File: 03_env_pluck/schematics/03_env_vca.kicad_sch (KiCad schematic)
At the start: 66 parts, among them J1 Eurorack 10 pin power connect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, J1 Gate In 1, J2 Signal in In 1, J3 Gate In 1, J4 Env Out 1, J4 signal out, J5 Env Out 1, Q1 BC547, Q2 BC547, SW1 Pluck / AD, SW2 Pluck / AD, U1 TL072, U2 LM324

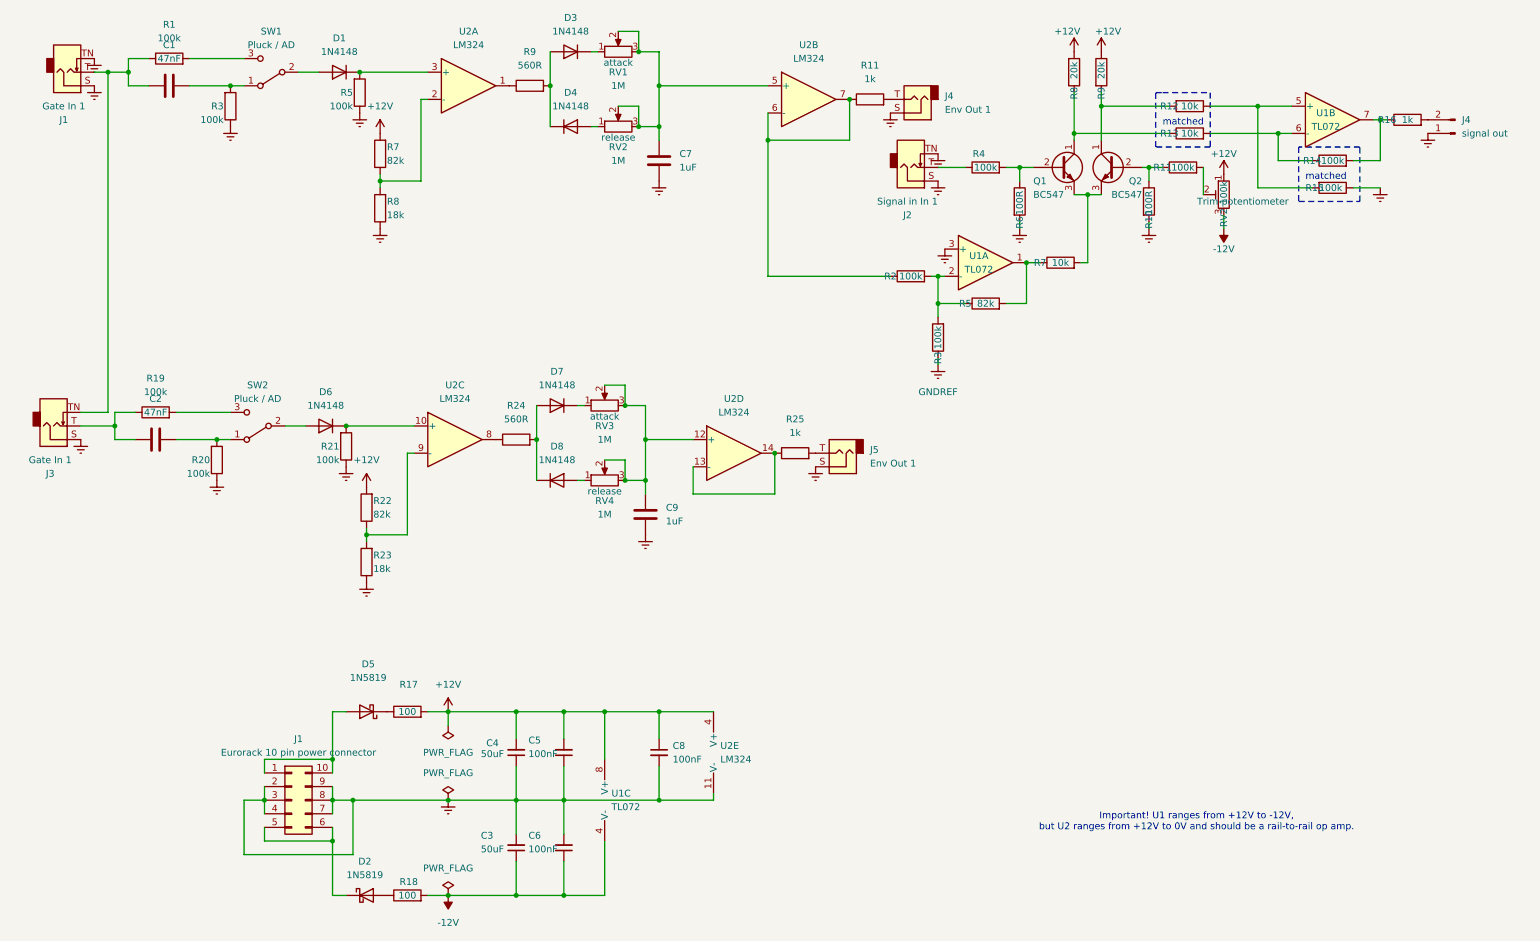
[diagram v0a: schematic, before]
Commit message: added PCB for 03
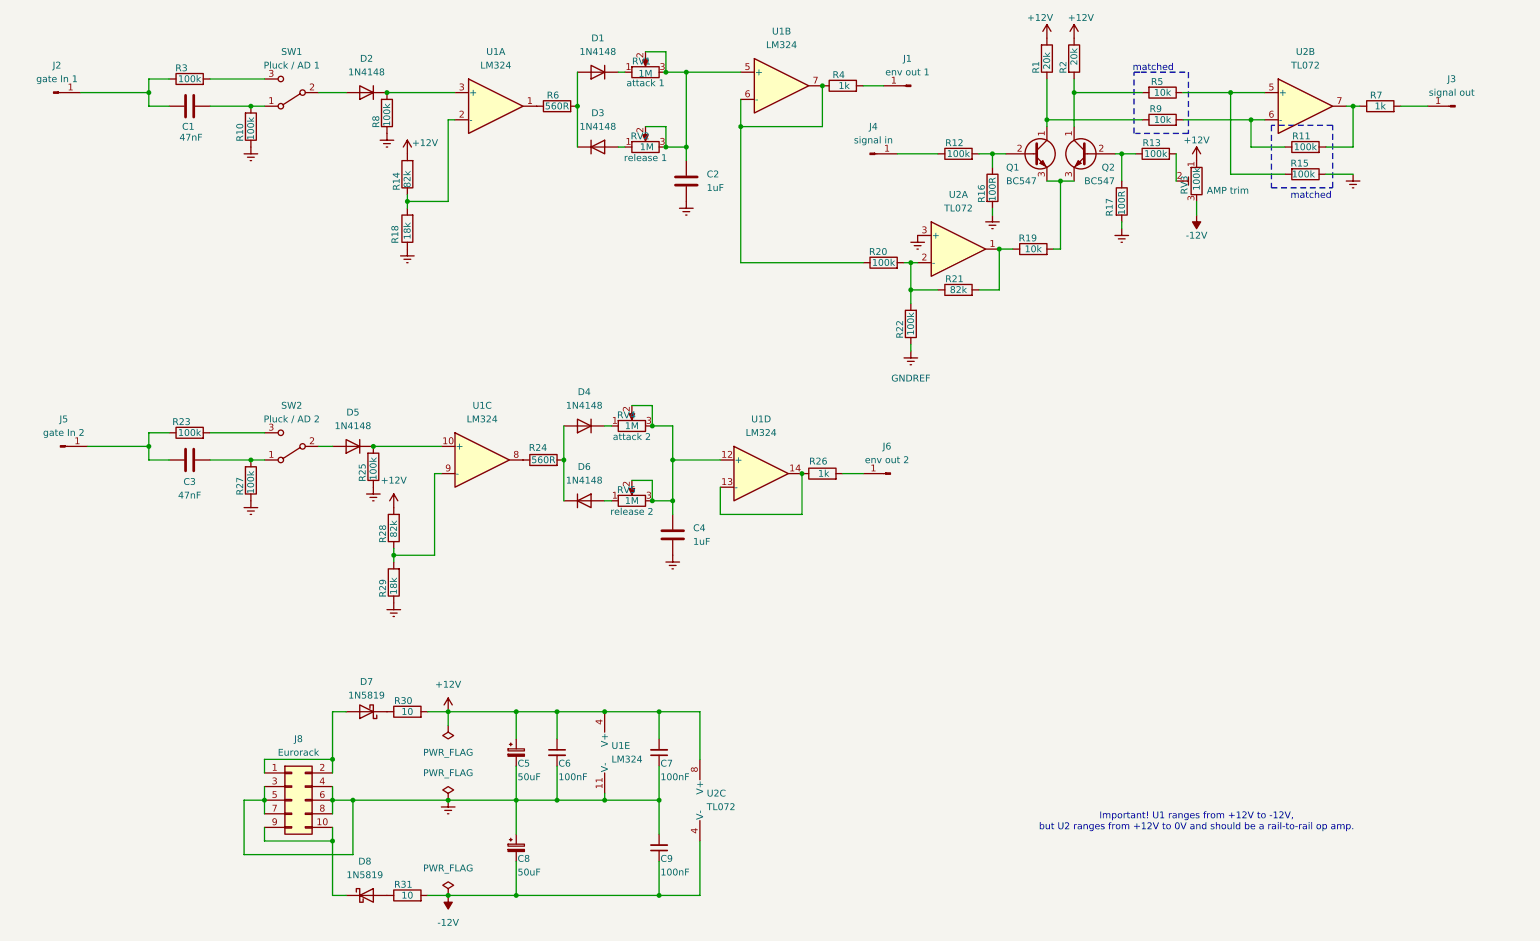
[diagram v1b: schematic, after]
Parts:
- removed C3, C4: 50uF, Capacitor_THT:C_Disc_D6.0mm_W2.5mm_P5.00mm, symbol Device:C_Small
- removed J1, J3: Gate In 1, Connector_Audio:Jack_6.35mm_Neutrik_NJ5FD-V_Vertical, symbol Connector_Audio:AudioJack2_SwitchT
- removed J1: Eurorack 10 pin power connector, Connector_PinHeader_2.54mm:PinHeader_2x05_P2.54mm_Vertical, symbol Connector_Generic:Conn_02x05_Counter_Clockwise
- removed J2: Signal in In 1, Connector_Audio:Jack_6.35mm_Neutrik_NJ5FD-V_Vertical, symbol Connector_Audio:AudioJack2_SwitchT
- removed J4, J5: Env Out 1, Connector_Audio:Jack_6.35mm_Neutrik_NJ5FD-V_Vertical, symbol Connector:AudioJack2
- removed J4: signal out, Connector_PinHeader_2.54mm:PinHeader_1x02_P2.54mm_Vertical, symbol Connector:Conn_01x02_Pin
- removed U1: TL072, Package_DIP:DIP-8_W7.62mm_Socket, symbol Amplifier_Operational:TL072
- added C5, C8: 50uF, Capacitor_THT:CP_Radial_D6.3mm_P2.50mm, symbol Device:C_Polarized_Small
- added J1: env out 1, Connector_PinHeader_2.54mm:PinHeader_1x01_P2.54mm_Vertical, symbol Connector:Conn_01x01_Pin
- added J2: gate In 1, Connector_PinHeader_2.54mm:PinHeader_1x01_P2.54mm_Vertical, symbol Connector:Conn_01x01_Pin
- added J3: signal out, Connector_PinHeader_2.54mm:PinHeader_1x01_P2.54mm_Vertical, symbol Connector:Conn_01x01_Pin
- added J4: signal in, Connector_PinHeader_2.54mm:PinHeader_1x01_P2.54mm_Vertical, symbol Connector:Conn_01x01_Pin
- added J5: gate In 2, Connector_PinHeader_2.54mm:PinHeader_1x01_P2.54mm_Vertical, symbol Connector:Conn_01x01_Pin
- added J6: env out 2, Connector_PinHeader_2.54mm:PinHeader_1x01_P2.54mm_Vertical, symbol Connector:Conn_01x01_Pin
- added J8: Eurorack, Connector_PinHeader_2.54mm:PinHeader_2x05_P2.54mm_Vertical, symbol Connector_Generic:Conn_02x05_Odd_Even
- added U2: TL072, Package_DIP:DIP-8_W7.62mm_Socket, symbol Amplifier_Operational:TL072
- R30: renamed from R17; value 100 -> 10
- R31: renamed from R18; value 100 -> 10
- RV1, RV2: footprint Potentiometer_THT:Potentiometer_Alpha_RD901F-40-00D_Single_Vertical -> Connector_PinHeader_2.54mm:PinHeader_1x03_P2.54mm_Vertical
- RV4: renamed from RV3; footprint Potentiometer_THT:Potentiometer_Alpha_RD901F-40-00D_Single_Vertical -> Connector_PinHeader_2.54mm:PinHeader_1x03_P2.54mm_Vertical
- RV5: renamed from RV4; footprint Potentiometer_THT:Potentiometer_Alpha_RD901F-40-00D_Single_Vertical -> Connector_PinHeader_2.54mm:PinHeader_1x03_P2.54mm_Vertical
- SW1: value Pluck / AD -> Pluck / AD 1
- SW2: value Pluck / AD -> Pluck / AD 2
- U1: renamed from U2; footprint (none) -> Package_DIP:DIP-14_W7.62mm_Socket
- renumbered C7 to C2, C2 to C3, C9 to C4, C8 to C6, C5 to C7, C6 to C9, D3 to D1, D1 to D2, D4 to D3, D7 to D4, D6 to D5, D8 to D6, D5 to D7, D2 to D8, R8 to R1, R3 to R10, R14 to R11, R4 to R12, R11 to R13, R7 to R14, R6 to R16, R10 to R17, R8 to R18, R7 to R19, R9 to R2, R2 to R20, R5 to R21, R3 to R22, R19 to R23, R21 to R25, R25 to R26, R20 to R27, R22 to R28, R23 to R29, R1 to R3, R11 to R4, R12 to R5, R9 to R6, R16 to R7, R5 to R8, R13 to R9, RV2 to RV3
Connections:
- net +12V: now also C5.1, U2.8 (V+)
- net -12V: now also C8.2, U2.4 (V-)
- net GNDREF: now also C5.2, C8.1, J8.3 (Pin_3), J8.4 (Pin_4), J8.5 (Pin_5), J8.6 (Pin_6), J8.7 (Pin_7), J8.8 (Pin_8), U2.3 (+)
- net at R19.1, R21.2: now also U2.1
- net at C3.1, R23.1: now also J5.1 (Pin_1)
- net at R20.2, R21.1, R22.2: now also U2.2 (-)
- net at R26.2: now also J6.1 (Pin_1)
- net at C1.1, R3.1: now also J2.1 (Pin_1)
- net at D7.2 (A): now also J8.1 (Pin_1), J8.2 (Pin_2)
- net at R12.1: now also J4.1 (Pin_1)
- net at R4.2: now also J1.1 (Pin_1)
- net at R11.1, R9.2: now also U2.6 (-)
- net at R11.2, R7.1: now also U2.7
- net at R7.2: now also J3.1 (Pin_1)
- net at R15.2, R5.1: now also U2.5 (+)
- net at D8.1 (K): now also J8.10 (Pin_10), J8.9 (Pin_9)
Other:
- moved on the sheet: C1, C2, C3, C4, C6, C7, C9, D1, D2, D3, D4, D5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

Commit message: updated PCBs for 02 and 03
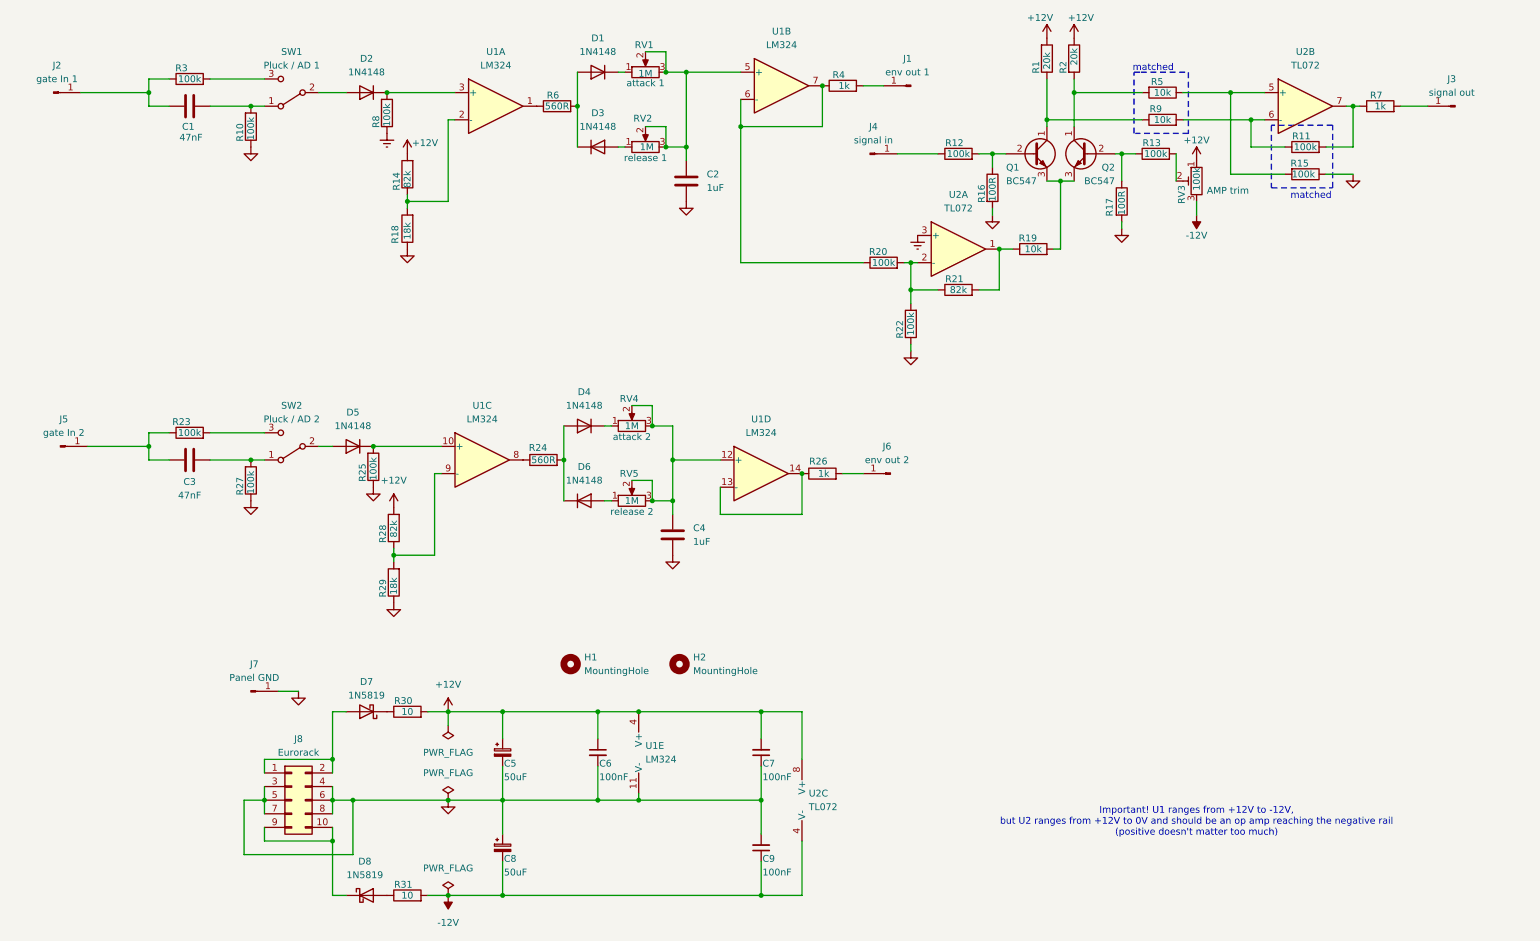
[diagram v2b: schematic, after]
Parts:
- added H1, H2: MountingHole, MountingHole:MountingHole_3.2mm_M3, symbol Mechanical:MountingHole
- added J7: Panel GND, Connector_PinHeader_2.54mm:PinHeader_1x01_P2.54mm_Vertical, symbol Connector:Conn_01x01_Pin
- C2, C4: footprint Capacitor_THT:C_Rect_L7.0mm_W2.5mm_P5.00mm -> Capacitor_THT:C_Rect_L7.2mm_W4.5mm_P5.00mm_FKS2_FKP2_MKS2_MKP2
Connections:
- net GNDREF: no longer C2.2, C4.2, C5.2, C6.2, C7.1, C8.1, C9.2, J8.3 (Pin_3), J8.4 (Pin_4), J8.5 (Pin_5), J8.6 (Pin_6), J8.7 (Pin_7), J8.8 (Pin_8), R10.1, R15.1, R16.2, R17.2, R18.1, R22.1, R25.1, R27.1, R29.1, U1.11 (V-)
- new net GND: C2.2, C4.2, C5.2, C6.2, C7.1, C8.1, C9.2, J7.1 (Pin_1), J8.3 (Pin_3), J8.4 (Pin_4), J8.5 (Pin_5), J8.6 (Pin_6), J8.7 (Pin_7), J8.8 (Pin_8), R10.1, R15.1, R16.2, R17.2, R18.1, R22.1, R25.1, R27.1, R29.1, U1.11 (V-)
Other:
- note added: "Important! U1 ranges from +12V to -12V, but U2 ranges from +12V to 0V and should be an op amp reaching the negative rail (positive doesn't matter too much)"
- note removed: "Important! U1 ranges from +12V to -12V, but U2 ranges from +12V to 0V and should be a rail-to-rail op amp."
- title: (none) -> mailman
- moved on the sheet: C5, C6, C7, C8, C9, U1E, U2C

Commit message: SMD baby
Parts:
- removed D7, D8: 1N5819, Diode_THT:D_DO-41_SOD81_P10.16mm_Horizontal, symbol Diode:1N5819
- removed H1, H2: MountingHole, MountingHole:MountingHole_3.2mm_M3, symbol Mechanical:MountingHole
- removed J1: env out 1, Connector_PinHeader_2.54mm:PinHeader_1x01_P2.54mm_Vertical, symbol Connector:Conn_01x01_Pin
- removed J2: gate In 1, Connector_PinHeader_2.54mm:PinHeader_1x01_P2.54mm_Vertical, symbol Connector:Conn_01x01_Pin
- removed J3: signal out, Connector_PinHeader_2.54mm:PinHeader_1x01_P2.54mm_Vertical, symbol Connector:Conn_01x01_Pin
- removed J4: signal in, Connector_PinHeader_2.54mm:PinHeader_1x01_P2.54mm_Vertical, symbol Connector:Conn_01x01_Pin
- removed J5: gate In 2, Connector_PinHeader_2.54mm:PinHeader_1x01_P2.54mm_Vertical, symbol Connector:Conn_01x01_Pin
- removed J6: env out 2, Connector_PinHeader_2.54mm:PinHeader_1x01_P2.54mm_Vertical, symbol Connector:Conn_01x01_Pin
- removed J7: Panel GND, Connector_PinHeader_2.54mm:PinHeader_1x01_P2.54mm_Vertical, symbol Connector:Conn_01x01_Pin
- removed R30, R31: 10, Resistor_THT:R_Axial_DIN0207_L6.3mm_D2.5mm_P10.16mm_Horizontal, symbol Device:R
- removed U1: LM324, Package_DIP:DIP-14_W7.62mm_Socket, symbol Amplifier_Operational:LM324
- added C8: 100nF, Capacitor_SMD:C_0805_2012Metric_Pad1.18x1.45mm_HandSolder, symbol Device:C_Small
- added J1: gate in 1, cynthia:3.5mm jack mono switched, symbol Connector_Audio:AudioJack2_SwitchT
- added J2: gate in 2, cynthia:3.5mm jack mono switched, symbol Connector_Audio:AudioJack2_SwitchT
- added J4: signal in, cynthia:3.5mm jack mono switched, symbol Connector_Audio:AudioJack2_SwitchT
- added J5: Env out 1, cynthia:3.5mm jack mono, symbol Connector_Audio:AudioJack2
- added J6: Env out 2, cynthia:3.5mm jack mono, symbol Connector_Audio:AudioJack2
- added J7: Signal out, cynthia:3.5mm jack mono, symbol Connector_Audio:AudioJack2
- added U1, U2: LM358, Package_SO:SOIC-8_3.9x4.9mm_P1.27mm, symbol Amplifier_Operational:LM358
- C1: footprint Capacitor_THT:C_Rect_L7.0mm_W2.5mm_P5.00mm -> Capacitor_SMD:C_0805_2012Metric_Pad1.18x1.45mm_HandSolder
- C10: renamed from C9; footprint Capacitor_THT:C_Disc_D6.0mm_W2.5mm_P5.00mm -> Capacitor_SMD:C_0805_2012Metric_Pad1.18x1.45mm_HandSolder
- C2: renamed from C3; footprint Capacitor_THT:C_Rect_L7.0mm_W2.5mm_P5.00mm -> Capacitor_SMD:C_0805_2012Metric_Pad1.18x1.45mm_HandSolder
- C5: renamed from C6; footprint Capacitor_THT:C_Disc_D7.5mm_W2.5mm_P5.00mm -> Capacitor_SMD:C_0805_2012Metric_Pad1.18x1.45mm_HandSolder
- C6: renamed from C4; footprint Capacitor_THT:C_Rect_L7.2mm_W4.5mm_P5.00mm_FKS2_FKP2_MKS2_MKP2 -> Capacitor_SMD:C_0805_2012Metric_Pad1.18x1.45mm_HandSolder
- C7: renamed from C2; footprint Capacitor_THT:C_Rect_L7.2mm_W4.5mm_P5.00mm_FKS2_FKP2_MKS2_MKP2 -> Capacitor_SMD:C_0805_2012Metric_Pad1.18x1.45mm_HandSolder
- C9: renamed from C7; footprint Capacitor_THT:C_Disc_D6.0mm_W2.5mm_P5.00mm -> Capacitor_SMD:C_0805_2012Metric_Pad1.18x1.45mm_HandSolder
- D1: renamed from D5; footprint Diode_THT:D_T-1_P10.16mm_Horizontal -> Diode_SMD:D_0805_2012Metric_Pad1.15x1.40mm_HandSolder
- D2: footprint Diode_THT:D_T-1_P10.16mm_Horizontal -> Diode_SMD:D_0805_2012Metric_Pad1.15x1.40mm_HandSolder
- D3: renamed from D4; footprint Diode_THT:D_T-1_P10.16mm_Horizontal -> Diode_SMD:D_0805_2012Metric_Pad1.15x1.40mm_HandSolder
- D4: renamed from D6; footprint Diode_THT:D_T-1_P10.16mm_Horizontal -> Diode_SMD:D_0805_2012Metric_Pad1.15x1.40mm_HandSolder
- D5: renamed from D1; footprint Diode_THT:D_T-1_P10.16mm_Horizontal -> Diode_SMD:D_0805_2012Metric_Pad1.15x1.40mm_HandSolder
- D6: renamed from D3; footprint Diode_THT:D_T-1_P10.16mm_Horizontal -> Diode_SMD:D_0805_2012Metric_Pad1.15x1.40mm_HandSolder
- Q1, Q2: footprint Package_TO_SOT_THT:TO-92_Inline -> Package_TO_SOT_SMD:SOT-23-3
- R1: renamed from R3; footprint Resistor_THT:R_Axial_DIN0207_L6.3mm_D2.5mm_P10.16mm_Horizontal -> Resistor_SMD:R_0805_2012Metric_Pad1.20x1.40mm_HandSolder
- R10: renamed from R18; footprint Resistor_THT:R_Axial_DIN0207_L6.3mm_D2.5mm_P10.16mm_Horizontal -> Resistor_SMD:R_0805_2012Metric_Pad1.20x1.40mm_HandSolder
- R11: renamed from R24; footprint Resistor_THT:R_Axial_DIN0207_L6.3mm_D2.5mm_P10.16mm_Horizontal -> Resistor_SMD:R_0805_2012Metric_Pad1.20x1.40mm_HandSolder
- R12: renamed from R6; footprint Resistor_THT:R_Axial_DIN0207_L6.3mm_D2.5mm_P10.16mm_Horizontal -> Resistor_SMD:R_0805_2012Metric_Pad1.20x1.40mm_HandSolder
- R13: renamed from R26; footprint Resistor_THT:R_Axial_DIN0207_L6.3mm_D2.5mm_P10.16mm_Horizontal -> Resistor_SMD:R_0805_2012Metric_Pad1.20x1.40mm_HandSolder
- R14: renamed from R4; footprint Resistor_THT:R_Axial_DIN0207_L6.3mm_D2.5mm_P10.16mm_Horizontal -> Resistor_SMD:R_0805_2012Metric_Pad1.20x1.40mm_HandSolder
- R15: renamed from R20; footprint Resistor_THT:R_Axial_DIN0207_L6.3mm_D2.5mm_P10.16mm_Horizontal -> Resistor_SMD:R_0805_2012Metric_Pad1.20x1.40mm_HandSolder
- R16: renamed from R22; footprint Resistor_THT:R_Axial_DIN0207_L6.3mm_D2.5mm_P10.16mm_Horizontal -> Resistor_SMD:R_0805_2012Metric_Pad1.20x1.40mm_HandSolder
- R17: renamed from R12; footprint Resistor_THT:R_Axial_DIN0207_L6.3mm_D2.5mm_P10.16mm_Horizontal -> Resistor_SMD:R_0805_2012Metric_Pad1.20x1.40mm_HandSolder
- R18: renamed from R21; footprint Resistor_THT:R_Axial_DIN0207_L6.3mm_D2.5mm_P10.16mm_Horizontal -> Resistor_SMD:R_0805_2012Metric_Pad1.20x1.40mm_HandSolder
- R19: renamed from R16; footprint Resistor_THT:R_Axial_DIN0207_L6.3mm_D2.5mm_P10.16mm_Horizontal -> Resistor_SMD:R_0805_2012Metric_Pad1.20x1.40mm_HandSolder
- R2: renamed from R23; footprint Resistor_THT:R_Axial_DIN0207_L6.3mm_D2.5mm_P10.16mm_Horizontal -> Resistor_SMD:R_0805_2012Metric_Pad1.20x1.40mm_HandSolder
- R20: renamed from R19; footprint Resistor_THT:R_Axial_DIN0207_L6.3mm_D2.5mm_P10.16mm_Horizontal -> Resistor_SMD:R_0805_2012Metric_Pad1.20x1.40mm_HandSolder
- R21: renamed from R1; footprint Resistor_THT:R_Axial_DIN0207_L6.3mm_D2.5mm_P10.16mm_Horizontal -> Resistor_SMD:R_0805_2012Metric_Pad1.20x1.40mm_HandSolder
- R22: renamed from R2; footprint Resistor_THT:R_Axial_DIN0207_L6.3mm_D2.5mm_P10.16mm_Horizontal -> Resistor_SMD:R_0805_2012Metric_Pad1.20x1.40mm_HandSolder
- R23: renamed from R17; footprint Resistor_THT:R_Axial_DIN0207_L6.3mm_D2.5mm_P10.16mm_Horizontal -> Resistor_SMD:R_0805_2012Metric_Pad1.20x1.40mm_HandSolder
- R24: renamed from R13; footprint Resistor_THT:R_Axial_DIN0207_L6.3mm_D2.5mm_P10.16mm_Horizontal -> Resistor_SMD:R_0805_2012Metric_Pad1.20x1.40mm_HandSolder
- R25: renamed from R5; footprint Resistor_THT:R_Axial_DIN0207_L6.3mm_D2.5mm_P10.16mm_Horizontal -> Resistor_SMD:R_0805_2012Metric_Pad1.20x1.40mm_HandSolder
- R26: renamed from R9; footprint Resistor_THT:R_Axial_DIN0207_L6.3mm_D2.5mm_P10.16mm_Horizontal -> Resistor_SMD:R_0805_2012Metric_Pad1.20x1.40mm_HandSolder
- R27: renamed from R11; footprint Resistor_THT:R_Axial_DIN0207_L6.3mm_D2.5mm_P10.16mm_Horizontal -> Resistor_SMD:R_0805_2012Metric_Pad1.20x1.40mm_HandSolder
- R28: renamed from R15; footprint Resistor_THT:R_Axial_DIN0207_L6.3mm_D2.5mm_P10.16mm_Horizontal -> Resistor_SMD:R_0805_2012Metric_Pad1.20x1.40mm_HandSolder
- R29: renamed from R7; footprint Resistor_THT:R_Axial_DIN0207_L6.3mm_D2.5mm_P10.16mm_Horizontal -> Resistor_SMD:R_0805_2012Metric_Pad1.20x1.40mm_HandSolder
- R3: renamed from R10; footprint Resistor_THT:R_Axial_DIN0207_L6.3mm_D2.5mm_P10.16mm_Horizontal -> Resistor_SMD:R_0805_2012Metric_Pad1.20x1.40mm_HandSolder
- R4: renamed from R27; footprint Resistor_THT:R_Axial_DIN0207_L6.3mm_D2.5mm_P10.16mm_Horizontal -> Resistor_SMD:R_0805_2012Metric_Pad1.20x1.40mm_HandSolder
- R5: renamed from R25; footprint Resistor_THT:R_Axial_DIN0207_L6.3mm_D2.5mm_P10.16mm_Horizontal -> Resistor_SMD:R_0805_2012Metric_Pad1.20x1.40mm_HandSolder
- R6: renamed from R8; footprint Resistor_THT:R_Axial_DIN0207_L6.3mm_D2.5mm_P10.16mm_Horizontal -> Resistor_SMD:R_0805_2012Metric_Pad1.20x1.40mm_HandSolder
- R7: renamed from R28; footprint Resistor_THT:R_Axial_DIN0207_L6.3mm_D2.5mm_P10.16mm_Horizontal -> Resistor_SMD:R_0805_2012Metric_Pad1.20x1.40mm_HandSolder
- R8: renamed from R29; footprint Resistor_THT:R_Axial_DIN0207_L6.3mm_D2.5mm_P10.16mm_Horizontal -> Resistor_SMD:R_0805_2012Metric_Pad1.20x1.40mm_HandSolder
- R9: renamed from R14; footprint Resistor_THT:R_Axial_DIN0207_L6.3mm_D2.5mm_P10.16mm_Horizontal -> Resistor_SMD:R_0805_2012Metric_Pad1.20x1.40mm_HandSolder
- RV1: renamed from RV4; footprint Connector_PinHeader_2.54mm:PinHeader_1x03_P2.54mm_Vertical -> cynthia:potientiometer
- RV2: renamed from RV5; footprint Connector_PinHeader_2.54mm:PinHeader_1x03_P2.54mm_Vertical -> cynthia:potientiometer
- RV3: renamed from RV1; footprint Connector_PinHeader_2.54mm:PinHeader_1x03_P2.54mm_Vertical -> cynthia:potientiometer
- RV4: renamed from RV2; footprint Connector_PinHeader_2.54mm:PinHeader_1x03_P2.54mm_Vertical -> cynthia:potientiometer
- RV5: renamed from RV3; footprint Potentiometer_THT:Potentiometer_Vishay_T73XW_Horizontal -> cynthia:trimmer
- SW1, SW2: footprint Connector_PinHeader_2.54mm:PinHeader_1x03_P2.54mm_Vertical -> cynthia:switch
- U3: renamed from U2; footprint Package_DIP:DIP-8_W7.62mm_Socket -> Package_SO:SOIC-8_3.9x4.9mm_P1.27mm
- renumbered C5 to C3, C8 to C4, J8 to J3
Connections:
- net +12V: now also J3.1 (Pin_1), J3.2 (Pin_2), C8.1, U1.8 (V+), U2.8 (V+)
- net -12V: now also J3.10 (Pin_10), J3.9 (Pin_9)
- net GND: now also R6.1, C8.2, J1.S, J1.TN, J2.S, J4.S, J4.TN, J5.S, J6.S, J7.S, U1.4 (V-), U2.4 (V-)
- net GNDREF: no longer R6.1
- net at D1.1 (K), R5.2: now also U1.5 (+)
- net at R11.1: now also U1.7
- net at R7.1, R8.2: now also U1.6 (-)
- net at C2.1, R2.1: now also J2.T
- net at R12.1: now also U2.7
- net at R29.2: now also J7.T
- net at R10.2, R9.1: now also U2.6 (-)
- net at C6.1, RV1.2, RV1.3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: now also U1.3 (+)
- net at R13.1: now also U1.1, U1.2 (-)
- net at R17.1: now also J4.T
- net at R13.2: now also J6.T
- net at R14.1, R15.1: now also U2.1, U2.2 (-)
- net at R14.2: now also J5.T
- net at C7.1, RV3.2, RV3.3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: now also U2.3 (+)
- net at C1.1, R1.1: now also J1.T, J2.TN
- net at D2.1 (K), R6.2: now also U2.5 (+)
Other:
- moved on the sheet: C10, C5, C9, U3C

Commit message: SMD baby 2
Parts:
- removed C2: 47nF, Capacitor_SMD:C_0805_2012Metric_Pad1.18x1.45mm_HandSolder, symbol Device:C
- removed C6: 1uF, Capacitor_SMD:C_0805_2012Metric_Pad1.18x1.45mm_HandSolder, symbol Device:C
- removed C8: 100nF, Capacitor_SMD:C_0805_2012Metric_Pad1.18x1.45mm_HandSolder, symbol Device:C_Small
- removed D1, D3, D4: 1N4148, Diode_SMD:D_0805_2012Metric_Pad1.15x1.40mm_HandSolder, symbol Device:D
- removed J2: gate in 2, cynthia:3.5mm jack mono switched, symbol Connector_Audio:AudioJack2_SwitchT
- removed J6: Env out 2, cynthia:3.5mm jack mono, symbol Connector_Audio:AudioJack2
- removed Q1, Q2: BC547, Package_TO_SOT_SMD:SOT-23-3, symbol Transistor_BJT:BC547
- removed R11: 560R, Resistor_SMD:R_0805_2012Metric_Pad1.20x1.40mm_HandSolder, symbol Device:R
- removed R13: 1k, Resistor_SMD:R_0805_2012Metric_Pad1.20x1.40mm_HandSolder, symbol Device:R
- removed R2, R4, R5: 100k, Resistor_SMD:R_0805_2012Metric_Pad1.20x1.40mm_HandSolder, symbol Device:R
- removed R7: 82k, Resistor_SMD:R_0805_2012Metric_Pad1.20x1.40mm_HandSolder, symbol Device:R
- removed R8: 18k, Resistor_SMD:R_0805_2012Metric_Pad1.20x1.40mm_HandSolder, symbol Device:R
- removed RV1, RV2: 1M, cynthia:potientiometer, symbol Device:R_Potentiometer
- removed SW2: Pluck / AD 2, cynthia:switch, symbol Switch:SW_SPDT
- removed U1: LM358, Package_SO:SOIC-8_3.9x4.9mm_P1.27mm, symbol Amplifier_Operational:LM358
- added Q1, Q2: BC847, Package_TO_SOT_SMD:SOT-23, symbol Transistor_BJT:BC847
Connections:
- net GNDREF is gone; now on net GND: U3.3 (+)
- net at R20.2: now also Q1.2 (E), Q2.2 (E)
- net at R17.2, R19.1: now also Q1.1 (B)
- net at R21.1, R26.1: now also Q1.3 (C)
- net at R22.2, R25.2: now also Q2.3 (C)
- net at R23.1, R24.1: now also Q2.1 (B)
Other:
- moved on the sheet: J4, J7, R15, R16, R17, R18, R19, R20, R21, R22, R23, R24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
